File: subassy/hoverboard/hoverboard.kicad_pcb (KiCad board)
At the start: 2 copper layers, 11 x 7 mm, 2 parts, among them J1 Conn_01x06_MountingPin, J2 Conn_02x05_Odd_Even

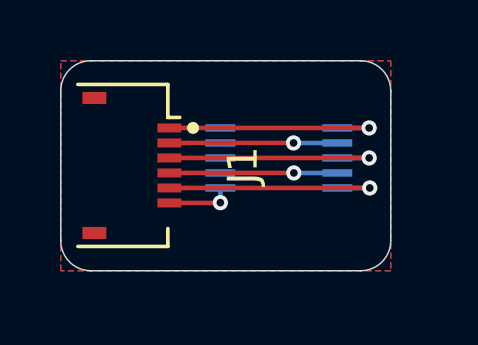
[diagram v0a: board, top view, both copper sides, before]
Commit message: Totally messed up the connections to the hoverboard
Great scott!!

Only caught this after placing an order at OSHpark.
Swiftly cancelled for this fix.

Signed-off-by: Michael Welling <mwelling@ieee.org>
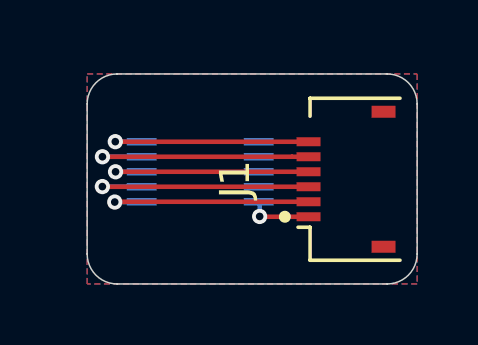
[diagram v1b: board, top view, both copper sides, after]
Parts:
- moved J1 7.15 mm to (153.5, 101.0), turned to 90 degrees
- moved J2 2.66 mm to (148.7, 100.7)
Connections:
- J1 pad 1: Net-(J1-Pad1) -> GND
- J1 pad 2: Net-(J1-Pad2) -> /VDD
- J1 pad 3: Net-(J1-Pad3) -> /INT
- J1 pad 4: Net-(J1-Pad4) -> /RST
- J1 pad 5: Net-(J1-Pad5) -> /SDA
- J1 pad 6: Net-(J1-Pad6) -> /SCL
- J2 pad 1: Net-(J1-Pad1) -> /SCL
- J2 pad 10: Net-(J1-Pad6) -> GND
- J2 pad 3: Net-(J1-Pad2) -> /SDA
- J2 pad 5: Net-(J1-Pad3) -> /RST
- J2 pad 7: Net-(J1-Pad4) -> /INT
- J2 pad 9: Net-(J1-Pad5) -> /VDD
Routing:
- net /SDA: track 0.00 -> 8.19 mm, vias 0 -> 1
- net /INT: track 0.00 -> 8.19 mm, vias 0 -> 1
- net Net-(J1-Pad5): track 7.76 -> 0.00 mm, vias 1 -> 0
- net Net-(J1-Pad3): track 7.72 -> 0.00 mm, vias 1 -> 0
- net Net-(J1-Pad1): track 7.72 -> 0.00 mm, vias 1 -> 0
- net /VDD: track 0.00 -> 7.37 mm, vias 0 -> 1
- net /SCL: track 0.00 -> 7.33 mm, vias 0 -> 1
- net /RST: track 0.00 -> 7.31 mm, vias 0 -> 1
- net Net-(J1-Pad2): track 5.60 -> 0.00 mm, vias 1 -> 0
- net Net-(J1-Pad4): track 5.60 -> 0.00 mm, vias 1 -> 0
- net Net-(J1-Pad6): track 2.19 -> 0.00 mm, vias 1 -> 0
- net GND: track 0.00 -> 2.15 mm, vias 0 -> 1
